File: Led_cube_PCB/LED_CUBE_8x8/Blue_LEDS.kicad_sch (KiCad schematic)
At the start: 2 parts, among them IC27 74AHC138PW,118

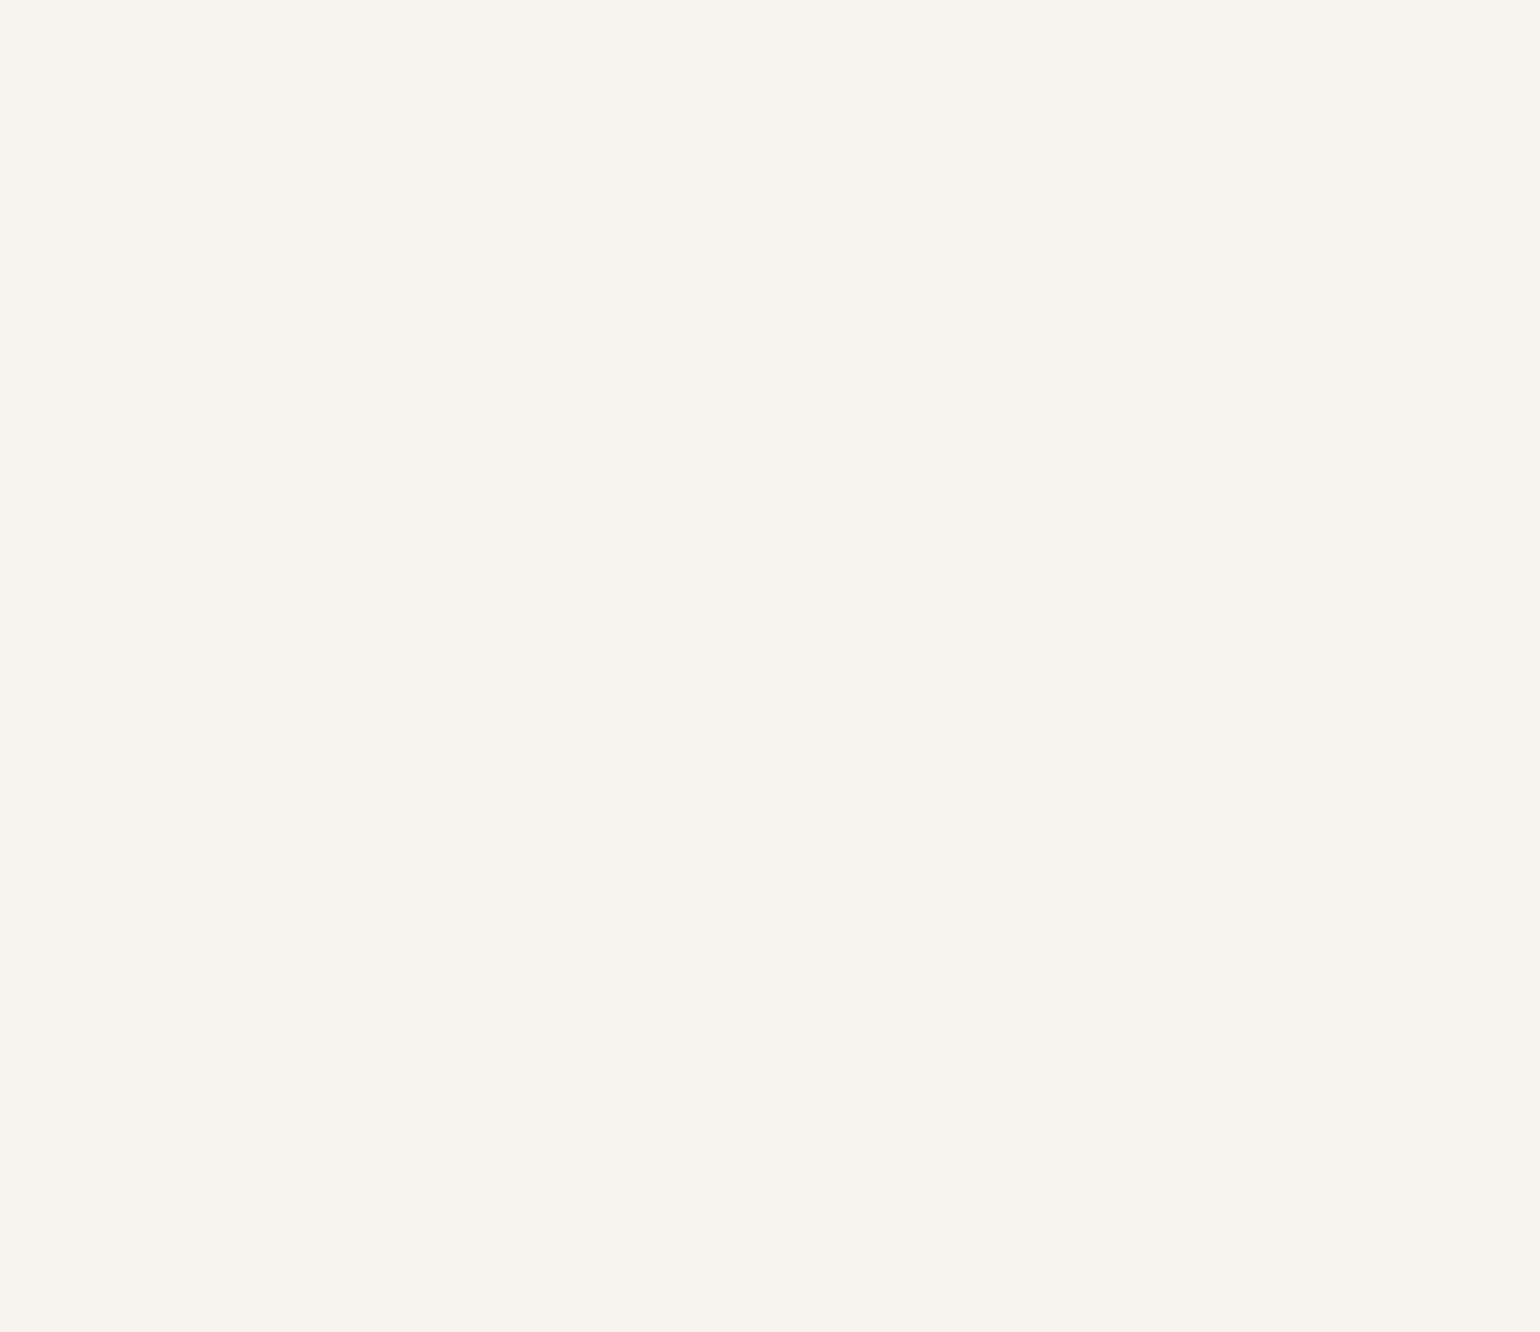
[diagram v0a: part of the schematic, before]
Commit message: Finished the schematic for the red green and blue color multiplexing.
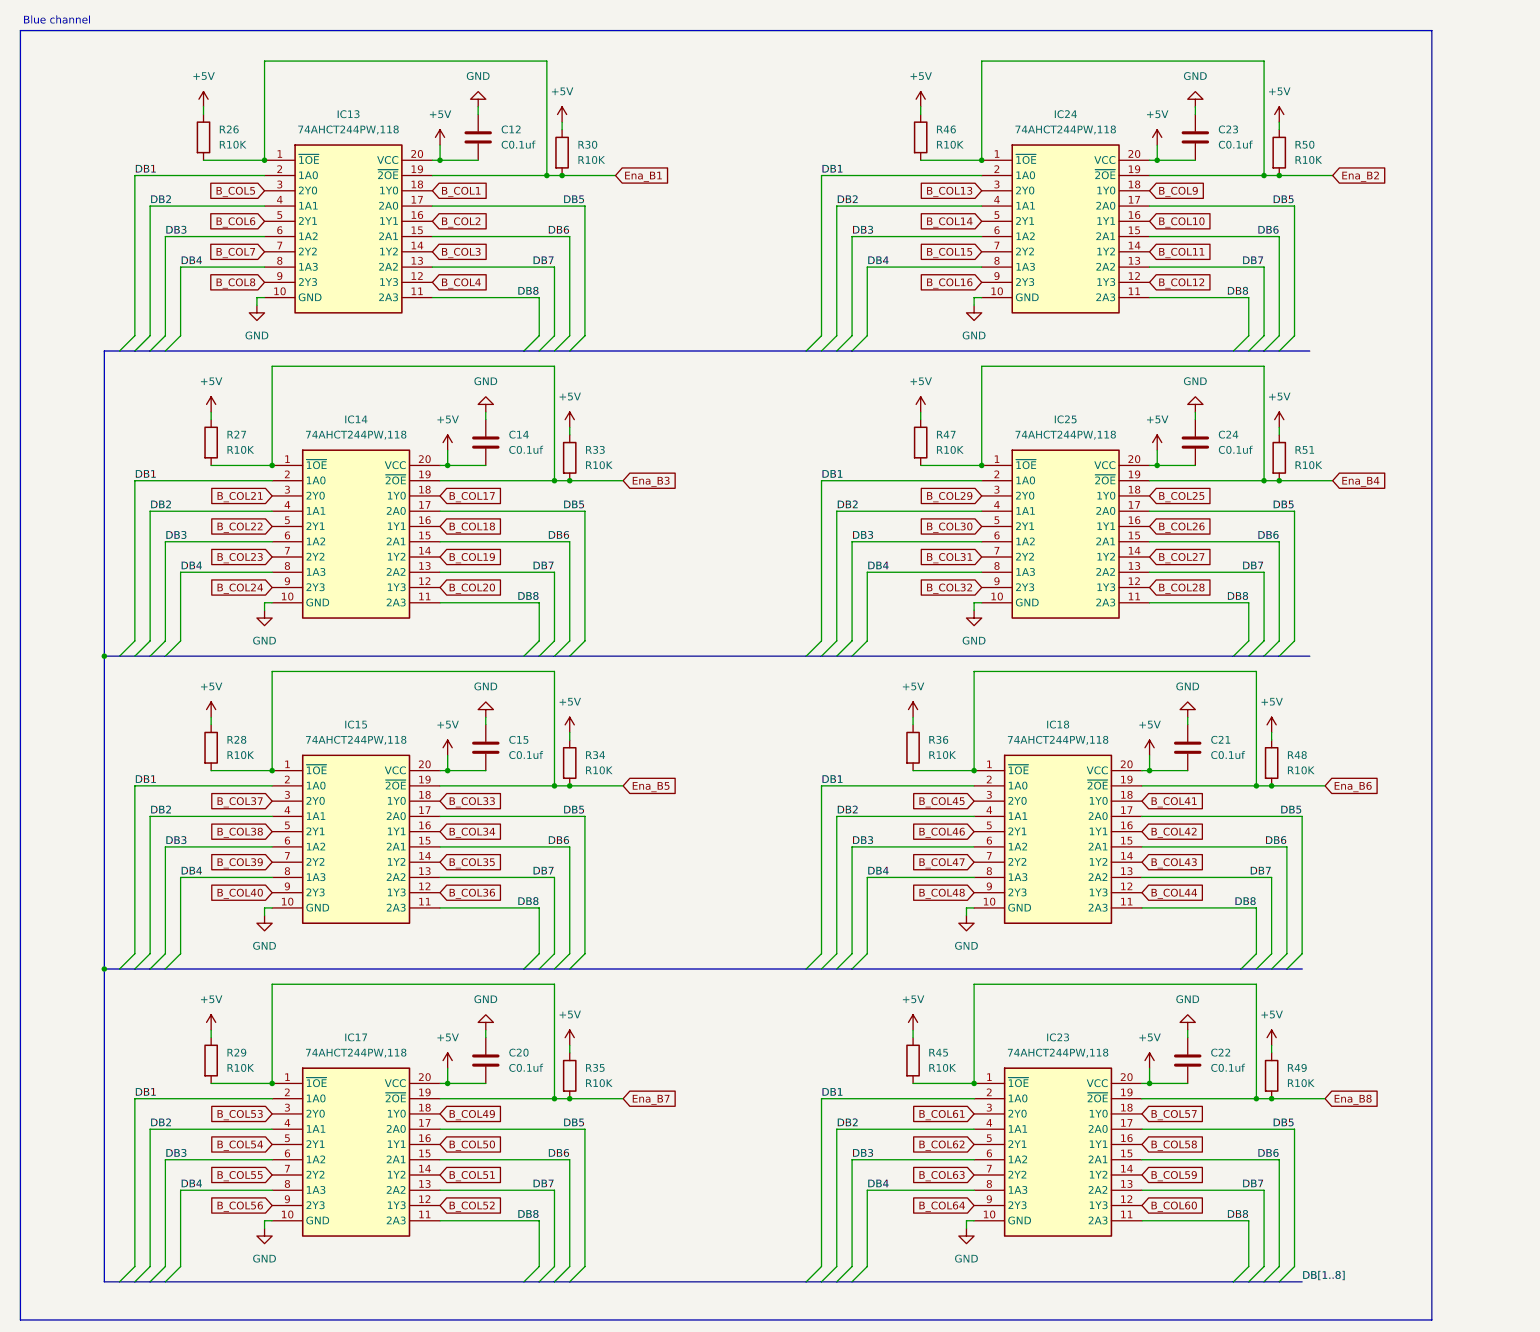
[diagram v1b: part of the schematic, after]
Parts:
- added C12, C14, C15, C20, C21, C22, C23, C24: C0.1uf, symbol Device:C
- added IC13, IC14, IC15, IC17, IC18, IC23, IC24, IC25: 74AHCT244PW,118, SOP65P640X110-20N, symbol SamacSys_Parts:74AHCT244PW,118
- added R26, R27, R28, R29, R30, R33, R34, R35, R36, R45, R46, R47, R48, R49, R50, R51: R10K, symbol Device:R
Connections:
- net +5V: now also C12.2, C14.2, C15.2, C20.2, C21.2, C22.2, C23.2, C24.2, IC13.20 (VCC), IC14.20 (VCC), IC15.20 (VCC), IC17.20 (VCC), IC18.20 (VCC), IC23.20 (VCC), IC24.20 (VCC), IC25.20 (VCC), R26.1, R27.1, R28.1, R29.1, R30.1, R33.1, R34.1, R35.1, R36.1, R45.1, R46.1, R47.1, R48.1, R49.1, R50.1, R51.1
- net Ena_B1: now also IC13.1 (~{1OE}), IC13.19 (~{2OE}), R26.2, R30.2
- net Ena_B2: now also IC24.1 (~{1OE}), IC24.19 (~{2OE}), R46.2, R50.2
- net Ena_B3: now also IC14.1 (~{1OE}), IC14.19 (~{2OE}), R27.2, R33.2
- net Ena_B4: now also IC25.1 (~{1OE}), IC25.19 (~{2OE}), R47.2, R51.2
- net Ena_B5: now also IC15.1 (~{1OE}), IC15.19 (~{2OE}), R28.2, R34.2
- net Ena_B6: now also IC18.1 (~{1OE}), IC18.19 (~{2OE}), R36.2, R48.2
- net Ena_B7: now also IC17.1 (~{1OE}), IC17.19 (~{2OE}), R29.2, R35.2
- net Ena_B8: now also IC23.1 (~{1OE}), IC23.19 (~{2OE}), R45.2, R49.2
- net GND: now also C12.1, C14.1, C15.1, C20.1, C21.1, C22.1, C23.1, C24.1, IC13.10 (GND), IC14.10 (GND), IC15.10 (GND), IC17.10 (GND), IC18.10 (GND), IC23.10 (GND), IC24.10 (GND), IC25.10 (GND)
- new net B_COL1: IC13.18 (1Y0)
- new net B_COL10: IC24.16 (1Y1)
- new net B_COL11: IC24.14 (1Y2)
- new net B_COL12: IC24.12 (1Y3)
- new net B_COL13: IC24.3 (2Y0)
- new net B_COL14: IC24.5 (2Y1)
- new net B_COL15: IC24.7 (2Y2)
- new net B_COL16: IC24.9 (2Y3)
- new net B_COL17: IC14.18 (1Y0)
- new net B_COL18: IC14.16 (1Y1)
- new net B_COL19: IC14.14 (1Y2)
- new net B_COL2: IC13.16 (1Y1)
- new net B_COL20: IC14.12 (1Y3)
- new net B_COL21: IC14.3 (2Y0)
- new net B_COL22: IC14.5 (2Y1)
- new net B_COL23: IC14.7 (2Y2)
- new net B_COL24: IC14.9 (2Y3)
- new net B_COL25: IC25.18 (1Y0)
- new net B_COL26: IC25.16 (1Y1)
- new net B_COL27: IC25.14 (1Y2)
- new net B_COL28: IC25.12 (1Y3)
- new net B_COL29: IC25.3 (2Y0)
- new net B_COL3: IC13.14 (1Y2)
- new net B_COL30: IC25.5 (2Y1)
- new net B_COL31: IC25.7 (2Y2)
- new net B_COL32: IC25.9 (2Y3)
- new net B_COL33: IC15.18 (1Y0)
- new net B_COL34: IC15.16 (1Y1)
- new net B_COL35: IC15.14 (1Y2)
- new net B_COL36: IC15.12 (1Y3)
- new net B_COL37: IC15.3 (2Y0)
- new net B_COL38: IC15.5 (2Y1)
- new net B_COL39: IC15.7 (2Y2)
- new net B_COL4: IC13.12 (1Y3)
- new net B_COL40: IC15.9 (2Y3)
- new net B_COL41: IC18.18 (1Y0)
- new net B_COL42: IC18.16 (1Y1)
- new net B_COL43: IC18.14 (1Y2)
- new net B_COL44: IC18.12 (1Y3)
- new net B_COL45: IC18.3 (2Y0)
- new net B_COL46: IC18.5 (2Y1)
- new net B_COL47: IC18.7 (2Y2)
- new net B_COL48: IC18.9 (2Y3)
- new net B_COL49: IC17.18 (1Y0)
- new net B_COL5: IC13.3 (2Y0)
- new net B_COL50: IC17.16 (1Y1)
- new net B_COL51: IC17.14 (1Y2)
- new net B_COL52: IC17.12 (1Y3)
- new net B_COL53: IC17.3 (2Y0)
- new net B_COL54: IC17.5 (2Y1)
- new net B_COL55: IC17.7 (2Y2)
- new net B_COL56: IC17.9 (2Y3)
- new net B_COL57: IC23.18 (1Y0)
- new net B_COL58: IC23.16 (1Y1)
- new net B_COL59: IC23.14 (1Y2)
- new net B_COL6: IC13.5 (2Y1)
- new net B_COL60: IC23.12 (1Y3)
- new net B_COL61: IC23.3 (2Y0)
- new net B_COL62: IC23.5 (2Y1)
- new net B_COL63: IC23.7 (2Y2)
- new net B_COL64: IC23.9 (2Y3)
- new net B_COL7: IC13.7 (2Y2)
- new net B_COL8: IC13.9 (2Y3)
- new net B_COL9: IC24.18 (1Y0)
- new net DB1: IC13.2 (1A0), IC14.2 (1A0), IC15.2 (1A0), IC17.2 (1A0), IC18.2 (1A0), IC23.2 (1A0), IC24.2 (1A0), IC25.2 (1A0)
- new net DB2: IC13.4 (1A1), IC14.4 (1A1), IC15.4 (1A1), IC17.4 (1A1), IC18.4 (1A1), IC23.4 (1A1), IC24.4 (1A1), IC25.4 (1A1)
- new net DB3: IC13.6 (1A2), IC14.6 (1A2), IC15.6 (1A2), IC17.6 (1A2), IC18.6 (1A2), IC23.6 (1A2), IC24.6 (1A2), IC25.6 (1A2)
- new net DB4: IC13.8 (1A3), IC14.8 (1A3), IC15.8 (1A3), IC17.8 (1A3), IC18.8 (1A3), IC23.8 (1A3), IC24.8 (1A3), IC25.8 (1A3)
- new net DB5: IC13.17 (2A0), IC14.17 (2A0), IC15.17 (2A0), IC17.17 (2A0), IC18.17 (2A0), IC23.17 (2A0), IC24.17 (2A0), IC25.17 (2A0)
- new net DB6: IC13.15 (2A1), IC14.15 (2A1), IC15.15 (2A1), IC17.15 (2A1), IC18.15 (2A1), IC23.15 (2A1), IC24.15 (2A1), IC25.15 (2A1)
- new net DB7: IC13.13 (2A2), IC14.13 (2A2), IC15.13 (2A2), IC17.13 (2A2), IC18.13 (2A2), IC23.13 (2A2), IC24.13 (2A2), IC25.13 (2A2)
- new net DB8: IC13.11 (2A3), IC14.11 (2A3), IC15.11 (2A3), IC17.11 (2A3), IC18.11 (2A3), IC23.11 (2A3), IC24.11 (2A3), IC25.11 (2A3)
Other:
- note added: "Blue channel"
- company: (none) -> Áuthor: Lars Molenschot
- title: Blue LED's -> 8x8_Led_Cube

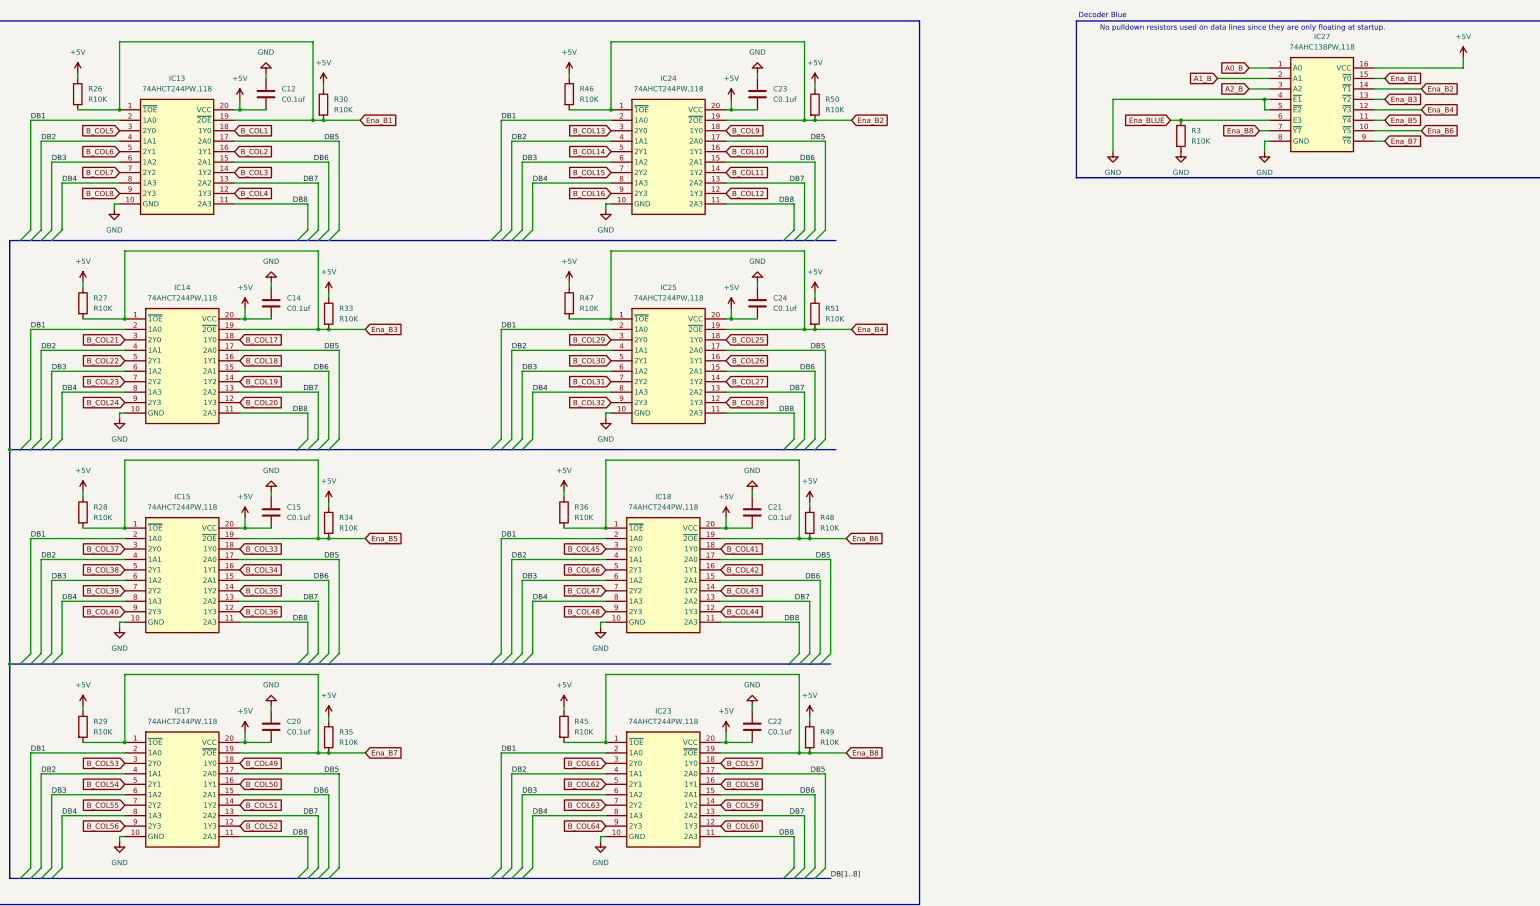
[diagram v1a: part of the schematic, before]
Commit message: added 3.3V power supply for microcontroller and started on STM schematic.
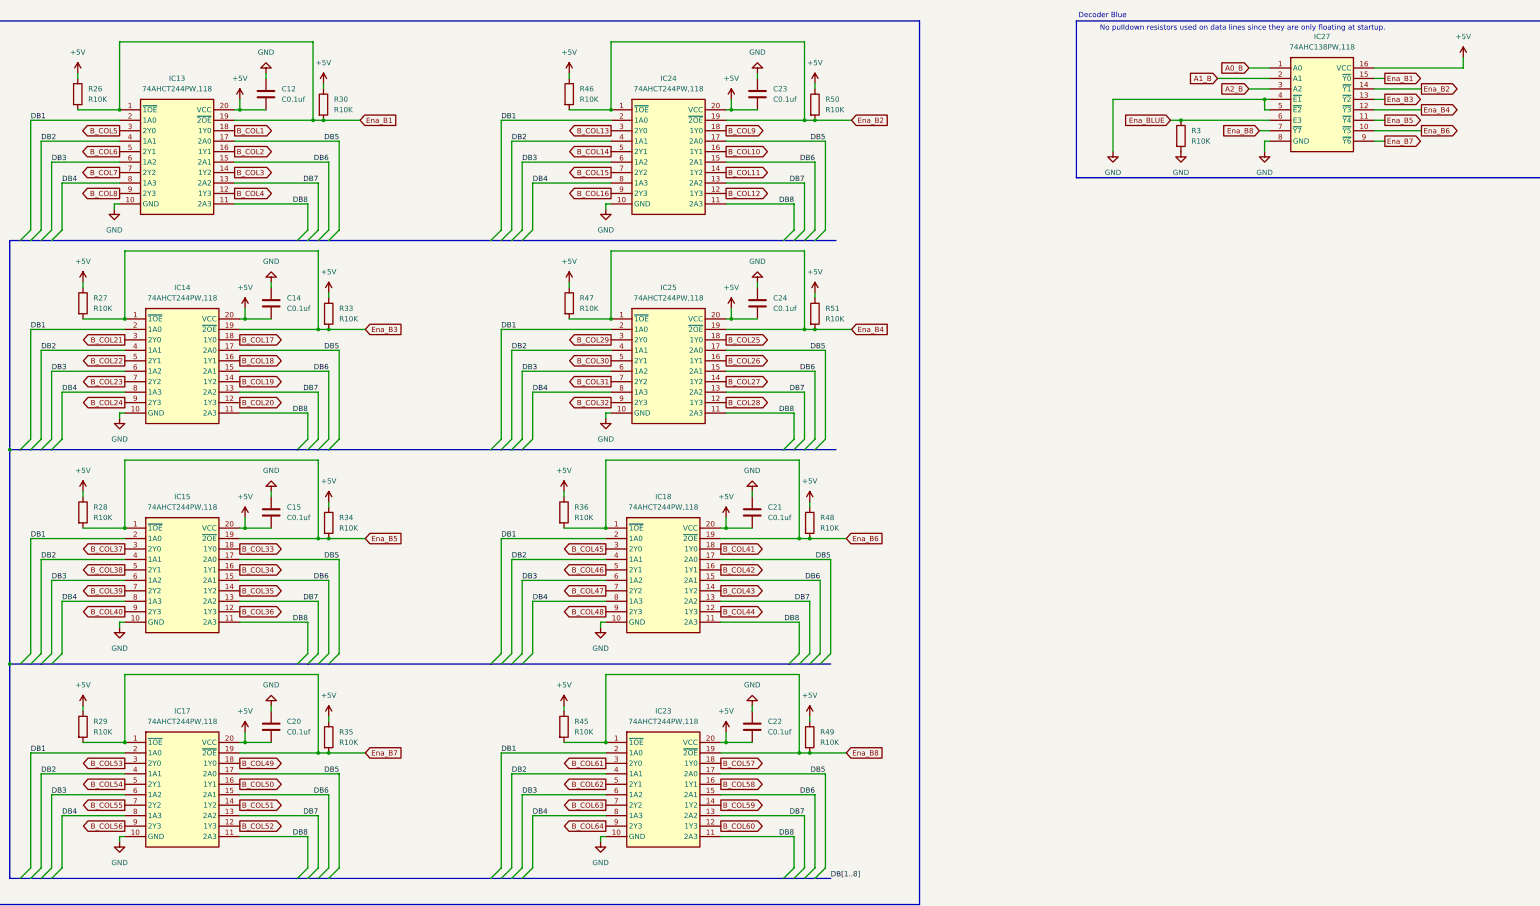
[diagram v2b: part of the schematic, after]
